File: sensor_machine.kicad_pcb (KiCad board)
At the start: 2 copper layers, 66 x 57.1 mm, 19 parts, among them J1 Barrel_Jack, J2 Barrel_Jack_Switch, J3 Screw_Terminal_01x02, J4 Screw_Terminal_01x02, J5 Screw_Terminal_01x02, J6 Screw_Terminal_01x02, U2 LM317_3PinPackage

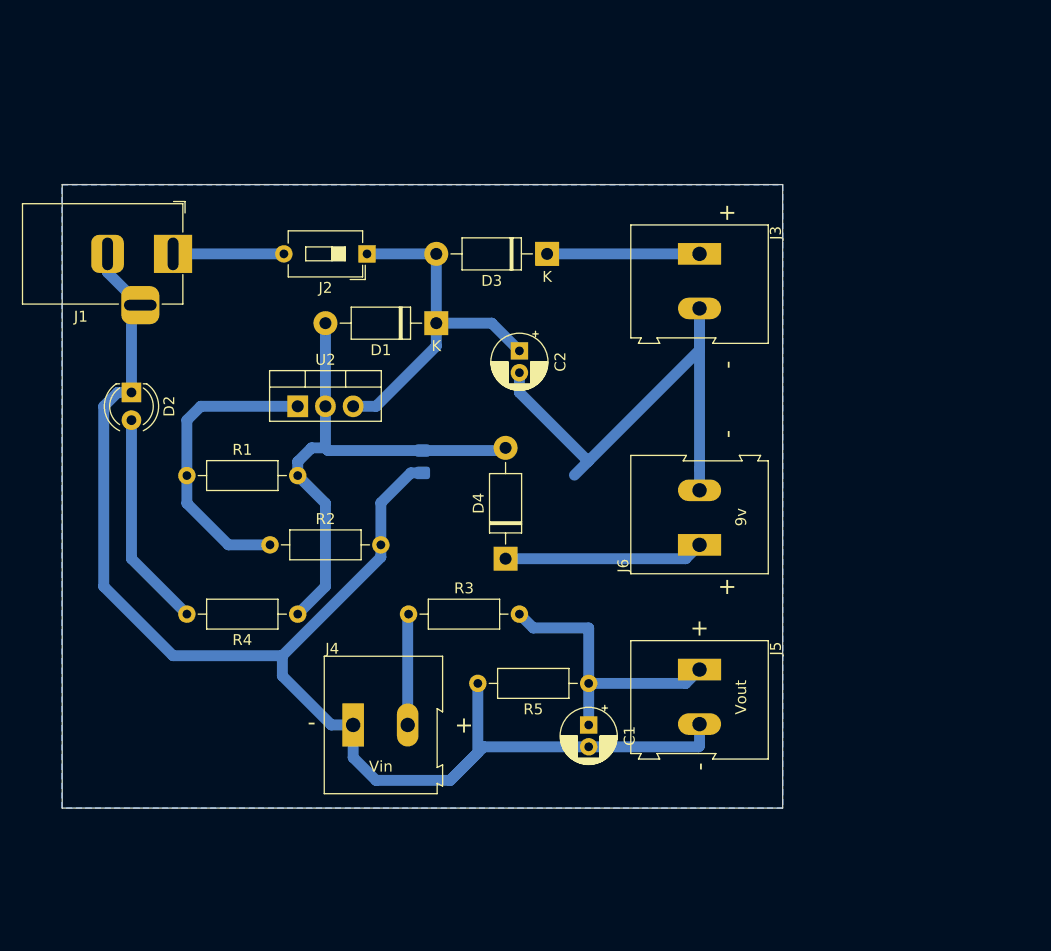
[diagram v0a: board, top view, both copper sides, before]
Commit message: modificaciones pcb con arduino UNO
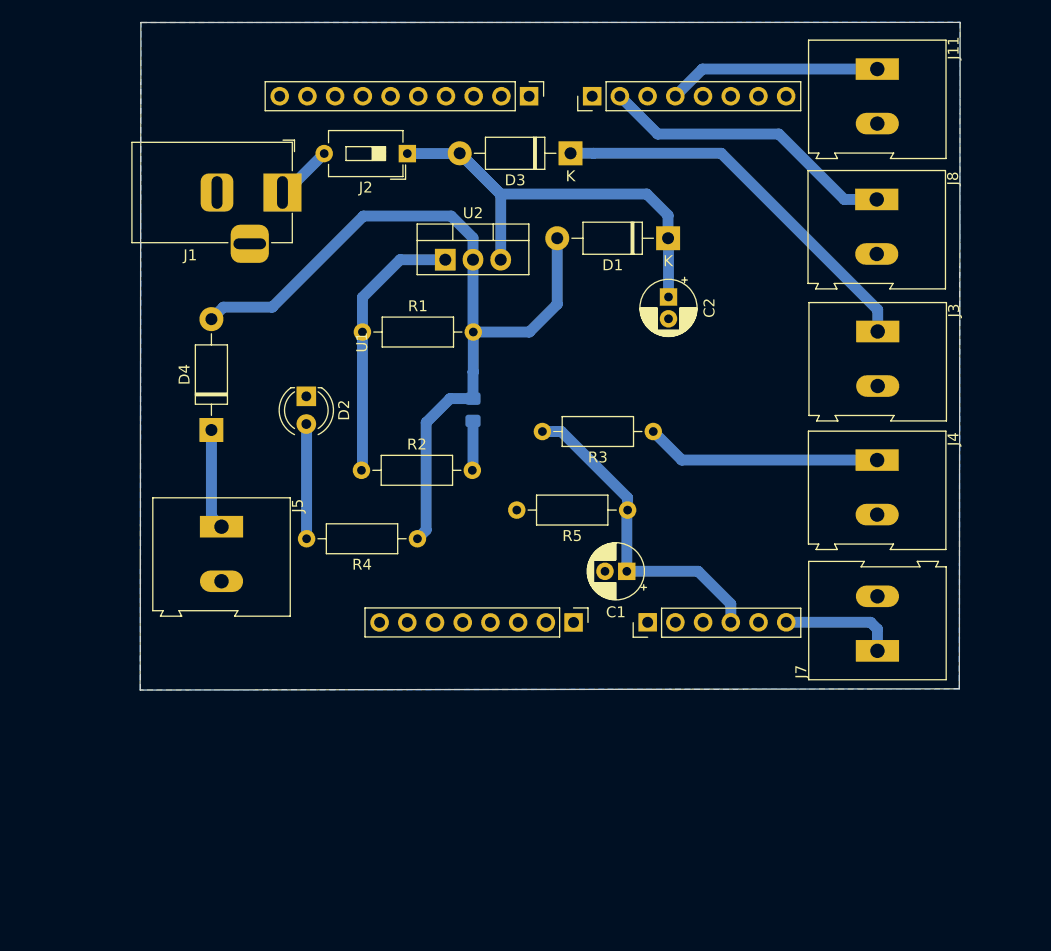
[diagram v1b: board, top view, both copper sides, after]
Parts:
- removed J6: Screw_Terminal_01x02, TerminalBlock:TerminalBlock_Altech_AK300-2_P5.00mm
- added J11: Screw_Terminal_01x02, TerminalBlock:TerminalBlock_Altech_AK300-2_P5.00mm, F.Cu at (180.1, 47.8)
- added J7: Screw_Terminal_01x02, TerminalBlock:TerminalBlock_Altech_AK300-2_P5.00mm, F.Cu at (180.1, 101.2)
- added J8: Screw_Terminal_01x02, TerminalBlock:TerminalBlock_Altech_AK300-2_P5.00mm, F.Cu at (180.1, 59.8)
- added U1: ard_UNO, ard_UNO:arduino_UNO, F.Cu at (146.0, 72.8)
- moved J4 53.8 mm to (180.1, 83.7), turned to 270 degrees
- moved J5 45.7 mm to (120.0, 89.8)
- moved D4 29.4 mm to (119.1, 80.9)
- moved R3 28.0 mm to (159.6, 81.1), turned to 180 degrees
- moved D1 22.6 mm to (160.9, 63.3)
- moved R1 20.8 mm to (132.9, 71.9)
- moved U2 19.1 mm to (140.5, 65.3)
- moved J3 17.8 mm to (180.2, 71.9)
- moved R5 16.3 mm to (157.2, 88.3)
- moved D2 16.0 mm to (127.8, 77.8)
- moved C2 14.5 mm to (161.0, 68.7)
- moved C1 14.5 mm to (157.2, 93.9), turned to 180 degrees
- moved R4 13.0 mm to (138.0, 90.9)
- moved J1 11.5 mm to (125.6, 59.1)
- moved R2 10.8 mm to (132.8, 84.6)
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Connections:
- C1 pad 1: Net-(C1-Pad1) -> /A3
- J4 pad 1: GND -> Net-(J4-Pad1)
- J4 pad 2: Net-(J4-Pad2) -> GND
- J5 pad 1: Net-(C1-Pad1) -> Net-(D4-Pad1)
- R3 pad 1: Net-(J4-Pad2) -> Net-(J4-Pad1)
- R3 pad 2: Net-(C1-Pad1) -> /A3
- R5 pad 1: Net-(C1-Pad1) -> /A3
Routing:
- net GND: track 182.0 -> 4.55 mm
- net /A3: track 0.00 -> 29.6 mm
- net /D6: track 0.00 -> 27.5 mm
- net +9V: track 47.3 -> 74.5 mm
- net Net-(C1-Pad1): track 26.5 -> 0.00 mm
- net Net-(D3-Pad1): track 14.0 -> 36.1 mm
- net Net-(J4-Pad1): track 0.00 -> 21.6 mm
- net /D4: track 0.00 -> 19.5 mm
- net +12V: track 33.4 -> 45.1 mm
- net /A5: track 0.00 -> 10.6 mm
- net Net-(J4-Pad2): track 10.2 -> 0.00 mm
- net Net-(D2-Pad2): track 19.9 -> 10.5 mm
- net Net-(D4-Pad1): track 18.3 -> 9.25 mm
- net Net-(J1-Pad1): track 10.2 -> 5.30 mm
- net Net-(R1-Pad1): track 27.5 -> 24.9 mm
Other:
- board size 66 x 57.1 mm -> 75.2 x 61.2 mm
- board text removed: "+"
- board text removed: "-"
- board text removed: "9v"
- board text removed: "Vin"
- board text removed: "Vout"

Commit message: reconfiguracion pcb
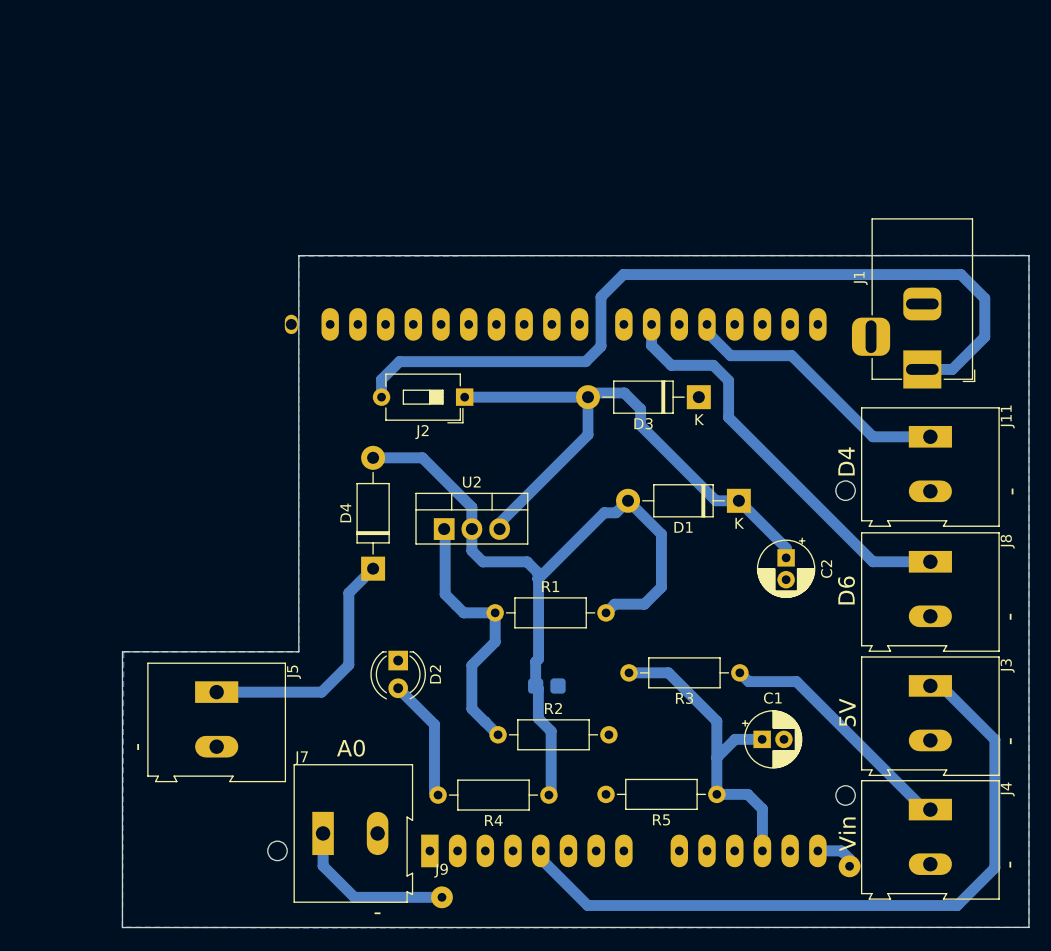
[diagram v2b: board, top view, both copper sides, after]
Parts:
- added ?: Screw_Terminal_01x01, Connector_Wire:SolderWirePad_1x01_Drill0.8mm, F.Cu at (177.6, 120.9)
- added J9: Screw_Terminal_01x01, Connector_Wire:SolderWirePad_1x01_Drill0.8mm, F.Cu at (140.2, 123.7)
- R2: value 120 -> 1200
- U1: footprint ard_UNO:arduino_UNO -> ard_UNO:Arduino_UNO_R3_WithMountingHoles_handsoldering; moved to B.Cu
- moved J1 60.8 mm to (184.3, 75.4), turned to 270 degrees
- moved J7 53.5 mm to (129.3, 117.9), turned to 0 degrees
- moved U1 47.2 mm to (139.1, 119.5), turned to 0 degrees
- moved J11 34.1 mm to (185.0, 81.5)
- moved J8 33.6 mm to (185.0, 93.0)
- moved J3 32.8 mm to (185.0, 104.4)
- moved J4 32.4 mm to (185.0, 115.7)
- moved R1 28.5 mm to (145.1, 97.7)
- moved R5 27.3 mm to (165.4, 114.3)
- moved R2 27.3 mm to (145.4, 108.9)
- moved R4 26.4 mm to (150.0, 114.4)
- moved C2 26.2 mm to (171.8, 92.6)
- moved C4 26.2 mm to (149.8, 104.4), turned to 0 degrees
- moved D2 25.6 mm to (136.2, 102.0)
- moved D3 25.3 mm to (163.8, 77.9)
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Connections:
- net +9V renamed +7.5V
- J3 pad 1: Net-(D3-Pad1) -> /5v
- J7 pad 1: /A5 -> Net-(J7-Pad1)
- U1 pad 14: /A5 -> Net-(J6-Pad1)
- U1 pad 5: Net-(U1-Pad5) -> /5v
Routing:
- net Net-(J1-Pad1): track 5.30 -> 74.9 mm
- net /5v: track 0.00 -> 65.3 mm
- net Net-(D3-Pad1): track 36.1 -> 0.00 mm
- net Net-(J7-Pad1): track 0.00 -> 15.1 mm
- net Net-(D4-Pad1): track 9.25 -> 22.9 mm
- net /A5: track 10.6 -> 0.00 mm
- net /D6: track 27.5 -> 37.7 mm
- net +12V: track 45.1 -> 52.7 mm
- net /D4: track 19.5 -> 25.1 mm
- net +7.5V: track 74.5 -> 69.5 mm
- net GND: track 4.55 -> 0.00 mm
- net Net-(J6-Pad1): track 0.00 -> 3.88 mm
- net Net-(J4-Pad1): track 21.6 -> 22.7 mm
- net Net-(D2-Pad2): track 10.5 -> 11.3 mm
- net Net-(R1-Pad1): track 24.9 -> 24.4 mm
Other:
- board size 75.2 x 61.2 mm -> 83.1 x 61.6 mm
- rule solder_mask_min_width: 0.25 -> 0.8
- board text added: "-"
- board text added: "5V"
- board text added: "A0"
- board text added: "D4"
- board text added: "D6"
- board text added: "Vin"
